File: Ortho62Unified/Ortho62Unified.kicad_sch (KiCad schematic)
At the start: 189 parts, among them J2 Conn_01x06_Socket, J3 USB_C_Receptacle_USB2.0, J5 Conn_01x06_Socket, J6 Conn_01x06_Socket, J7 Conn_01x08_Socket, J8 Conn_01x06_Socket, J9 TC2030-IDC-NL, SW1 SW_Push, SW10 SW_Push, SW11 SW_Push, SW12 SW_Push, SW13 SW_Push, SW14 SW_Push, SW15 SW_Push, SW16 SW_Push, SW17 SW_Push, SW18 SW_Push, SW19 SW_Push, SW2 SW_Push, SW20 SW_Push, SW21 SW_Push, SW22 SW_Push, SW23 SW_Push, SW24 SW_Push, SW25 SW_Push, SW26 SW_Push, SW27 SW_Push, SW28 SW_Push, SW29 SW_Push, SW3 SW_Push, SW30 SW_Push, SW31 SW_Push, SW32 SW_Push, SW33 SW_Push, SW34 SW_Push, SW35 SW_Push, SW36 SW_Push, SW37 SW_Push, SW38 SW_Push, SW39 SW_Push, SW4 SW_Push, SW40 SW_Push, SW41 SW_Push, SW42 SW_Push, SW43 SW_Push, SW44 SW_Push, SW45 SW_Push, SW46 SW_Push, SW47 SW_Push, SW48 SW_Push, SW49 SW_Push, SW5 SW_Push, SW50 SW_Push, SW51 SW_Push, SW52 SW_Push, SW53 SW_Push, SW54 SW_Push, SW55 SW_Push, SW56 SW_Push, SW57 SW_Push, SW58 SW_Push, SW59 SW_Push, SW6 SW_Push, SW60 SW_Push, SW61 SW_Push, SW62 SW_Push, SW63 SW_Push, SW64 SW_Push, SW65 SW_Push, SW66 SW_Push, SW67 SW_Push, SW68 SW_Push, SW69 SW_Push, SW7 SW_Push, SW70 SW_Push, SW71 SW_Push, SW72 SW_Push, SW73 SW_Push, SW74 OS, SW75 SW_Push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

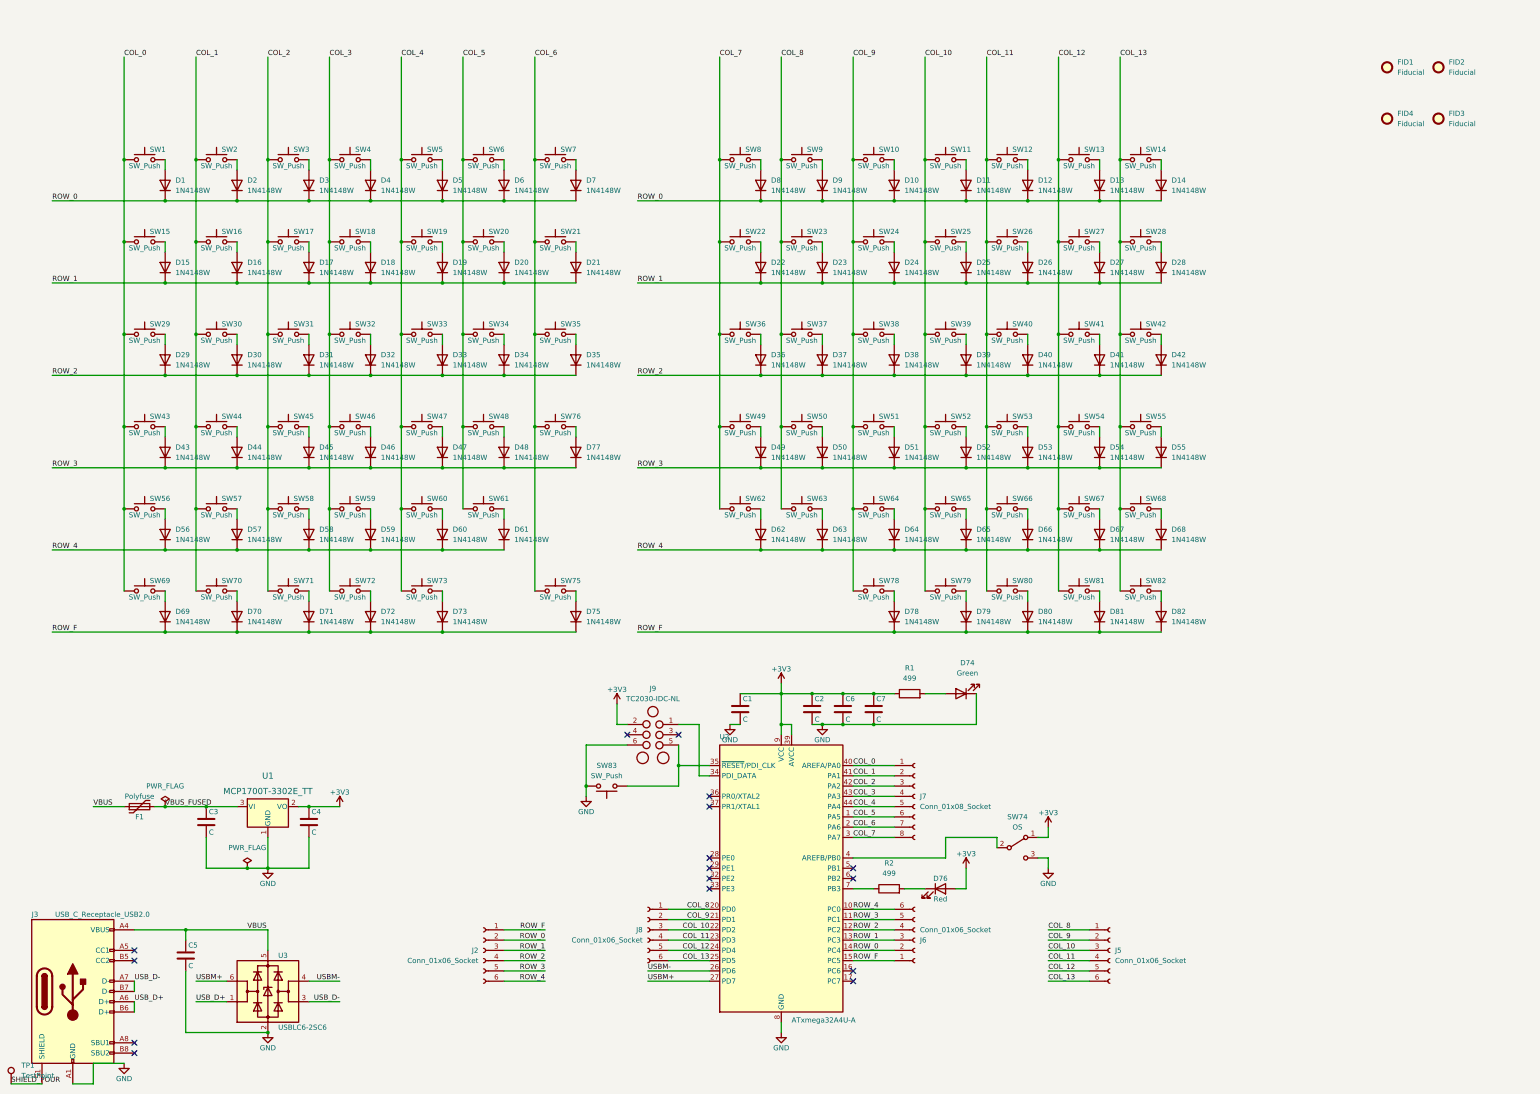
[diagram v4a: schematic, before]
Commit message: Correct spacing and kb2040 try.
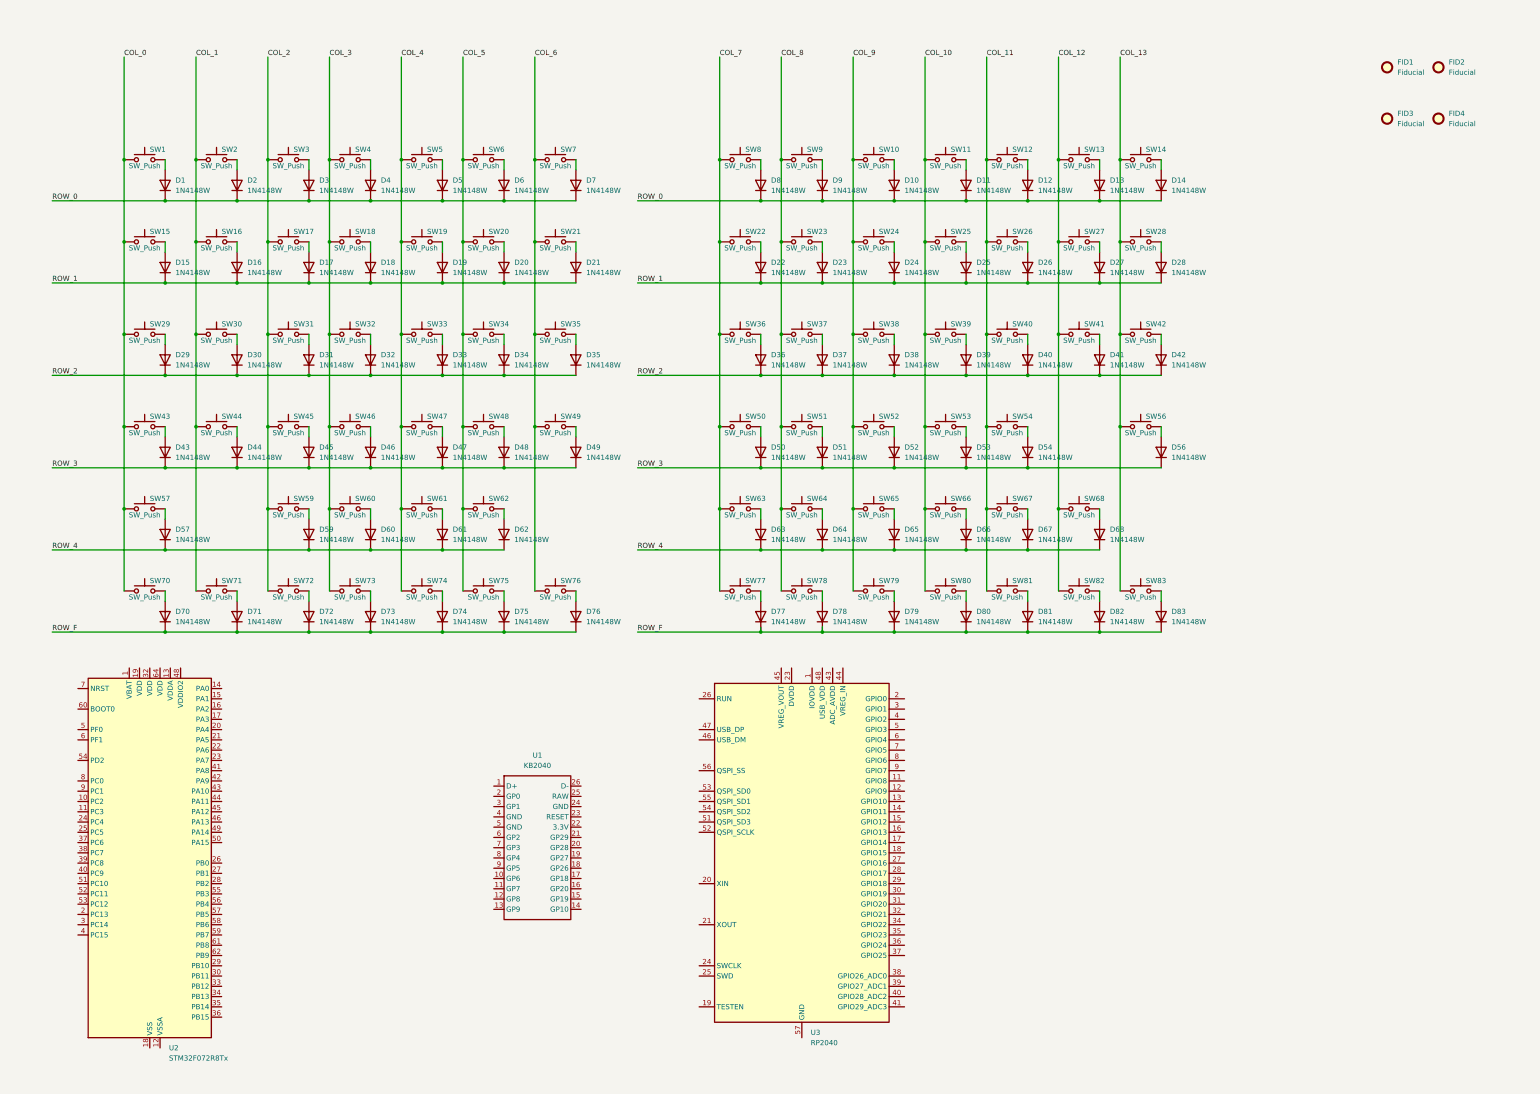
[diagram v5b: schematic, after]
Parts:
- removed C1, C2, C3, C4, C5, C6, C7: C, Capacitor_SMD:C_0603_1608Metric_Pad1.08x0.95mm_HandSolder, symbol Device:C
- removed D54, D57, D68: 1N4148W, Diode_SMD:D_SOD-123, symbol Diode:1N4148W
- removed D74: Green, LED_SMD:LED_0805_2012Metric_Pad1.15x1.40mm_HandSolder, symbol Device:LED
- removed D76: Red, LED_SMD:LED_0805_2012Metric_Pad1.15x1.40mm_HandSolder, symbol Device:LED
- removed F1: Polyfuse, Fuse:Fuse_1206_3216Metric_Pad1.42x1.75mm_HandSolder, symbol Device:Polyfuse
- removed J2, J5, J6, J8: Conn_01x06_Socket, Connector_PinHeader_1.27mm:PinHeader_1x06_P1.27mm_Vertical, symbol Connector:Conn_01x06_Socket
- removed J3: USB_C_Receptacle_USB2.0, CustomHandSolderConnectors:USB_C_Receptacle_GCT_USB4085_HandSolder_SMT, symbol Connector:USB_C_Receptacle_USB2.0
- removed J7: Conn_01x08_Socket, Connector_PinHeader_1.27mm:PinHeader_1x08_P1.27mm_Vertical, symbol Connector:Conn_01x08_Socket
- removed J9: TC2030-IDC-NL, Tag_Connect:TC2030-IDC-NL, symbol Tag-Connect:TC2030-IDC-NL
- removed R1: 499, Resistor_SMD:R_0805_2012Metric_Pad1.20x1.40mm_HandSolder, symbol Device:R
- removed R2: 499, LED_SMD:LED_0805_2012Metric_Pad1.15x1.40mm_HandSolder, symbol Device:R
- removed SW54, SW57, SW68: SW_Push, Switch_Keyboard_Kailh:SW_Kailh_Choc_V1V2_1.00u, symbol Switch:SW_Push
- removed SW74: OS, Button_Switch_SMD:SW_SPDT_CK-JS102011SAQN, symbol Switch:SW_SPDT
- removed SW83: SW_Push, Button_Switch_SMD:SW_Tactile_SPST_NO_Straight_CK_PTS636Sx25SMTRLFS, symbol Switch:SW_Push
- removed TP1: TestPoint, TestPoint:TestPoint_Pad_D1.0mm, symbol Connector:TestPoint
- removed U1: MCP1700T-3302E_TT, Package_TO_SOT_SMD:SOT-23, symbol Regulator_Linear:MCP1700x-330xxTT
- removed U2: ATxmega32A4U-A, Package_QFP:TQFP-44_10x10mm_P0.8mm, symbol MCU_Microchip_ATmega:ATxmega32A4U-A
- removed U3: USBLC6-2SC6, Package_TO_SOT_SMD:SOT-23-6, symbol Power_Protection:USBLC6-2SC6
- added D75, D77, D78: 1N4148W, Diode_SMD:D_SOD-123, symbol Diode:1N4148W
- added SW75, SW77, SW78: SW_Push, Kailh Keyboard Switches:SW_Kailh_Choc_V1V2_1.00u, symbol Switch:SW_Push
- added U1: KB2040, KB2040:Adafruit_KB2040, symbol KB2040:KB2040
- added U2: STM32F072R8Tx, Package_QFP:LQFP-64_10x10mm_P0.5mm, symbol MCU_ST_STM32F0:STM32F072R8Tx
- added U3: RP2040, Package_DFN_QFN:QFN-56-1EP_7x7mm_P0.4mm_EP3.2x3.2mm, symbol MCU_RaspberryPi:RP2040
- SW1, SW10, SW11, SW12, SW13, SW15, SW16, SW17, SW18, SW19, SW2, SW20, SW22, SW23, SW24, SW25, SW26, SW27, SW29, SW3, SW30, SW31, SW32, SW33, SW34, SW36, SW37, SW38, SW39, SW4, SW40, SW41, SW43, SW44, SW45, SW46, SW47, SW48, SW5, SW6, SW8, SW9: footprint Switch_Keyboard_Kailh:SW_Kailh_Choc_V1V2_1.00u -> Kailh Keyboard Switches:SW_Kailh_Choc_V1V2_1.00u
- SW14, SW21, SW28, SW35, SW42, SW7: footprint Switch_Keyboard_Kailh:SW_Kailh_Choc_V1V2_1.50u -> Kailh Keyboard Switches:SW_Kailh_Choc_V1V2_1.50u
- SW49: renamed from SW76; footprint Switch_Keyboard_Kailh:SW_Kailh_Choc_V1V2_1.00u -> Kailh Keyboard Switches:SW_Kailh_Choc_V1V2_1.00u
- SW50: renamed from SW49; footprint Switch_Keyboard_Kailh:SW_Kailh_Choc_V1V2_1.00u -> Kailh Keyboard Switches:SW_Kailh_Choc_V1V2_1.00u
- SW51: renamed from SW50; footprint Switch_Keyboard_Kailh:SW_Kailh_Choc_V1V2_1.00u -> Kailh Keyboard Switches:SW_Kailh_Choc_V1V2_1.00u
- SW52: renamed from SW51; footprint Switch_Keyboard_Kailh:SW_Kailh_Choc_V1V2_1.00u -> Kailh Keyboard Switches:SW_Kailh_Choc_V1V2_1.00u
- SW53: renamed from SW52; footprint Switch_Keyboard_Kailh:SW_Kailh_Choc_V1V2_1.00u -> Kailh Keyboard Switches:SW_Kailh_Choc_V1V2_1.00u
- SW54: renamed from SW53; footprint Switch_Keyboard_Kailh:SW_Kailh_Choc_V1V2_1.00u -> Kailh Keyboard Switches:SW_Kailh_Choc_V1V2_1.00u
- SW56: renamed from SW55; footprint Switch_Keyboard_Kailh:SW_Kailh_Choc_V1V2_1.00u -> Kailh Keyboard Switches:SW_Kailh_Choc_V1V2_2.00u
- SW57: renamed from SW56; footprint Switch_Keyboard_Kailh:SW_Kailh_Choc_V1V2_1.50u -> Kailh Keyboard Switches:SW_Kailh_Choc_V1V2_2.00u
- SW59: renamed from SW58; footprint Switch_Keyboard_Kailh:SW_Kailh_Choc_V1V2_1.00u -> Kailh Keyboard Switches:SW_Kailh_Choc_V1V2_1.00u
- SW60: renamed from SW59; footprint Switch_Keyboard_Kailh:SW_Kailh_Choc_V1V2_1.00u -> Kailh Keyboard Switches:SW_Kailh_Choc_V1V2_1.00u
- SW61: renamed from SW60; footprint Switch_Keyboard_Kailh:SW_Kailh_Choc_V1V2_1.00u -> Kailh Keyboard Switches:SW_Kailh_Choc_V1V2_1.00u
- SW62: renamed from SW61; footprint Switch_Keyboard_Kailh:SW_Kailh_Choc_V1V2_1.50u -> Kailh Keyboard Switches:SW_Kailh_Choc_V1V2_1.50u
- SW63: renamed from SW62; footprint Switch_Keyboard_Kailh:SW_Kailh_Choc_V1V2_1.00u -> Kailh Keyboard Switches:SW_Kailh_Choc_V1V2_1.00u
- SW64: renamed from SW63; footprint Switch_Keyboard_Kailh:SW_Kailh_Choc_V1V2_1.50u -> Kailh Keyboard Switches:SW_Kailh_Choc_V1V2_1.50u
- SW65: renamed from SW64; footprint Switch_Keyboard_Kailh:SW_Kailh_Choc_V1V2_1.00u -> Kailh Keyboard Switches:SW_Kailh_Choc_V1V2_1.00u
- SW66: renamed from SW65; footprint Switch_Keyboard_Kailh:SW_Kailh_Choc_V1V2_1.00u -> Kailh Keyboard Switches:SW_Kailh_Choc_V1V2_1.00u
- SW67: renamed from SW66; footprint Switch_Keyboard_Kailh:SW_Kailh_Choc_V1V2_1.00u -> Kailh Keyboard Switches:SW_Kailh_Choc_V1V2_1.00u
- SW68: renamed from SW67; footprint Switch_Keyboard_Kailh:SW_Kailh_Choc_V1V2_1.50u -> Kailh Keyboard Switches:SW_Kailh_Choc_V1V2_1.50u
- SW70: renamed from SW69; footprint Switch_Keyboard_Kailh:SW_Kailh_Choc_V1V2_1.00u -> Kailh Keyboard Switches:SW_Kailh_Choc_V1V2_1.00u
- SW71: renamed from SW70; footprint Switch_Keyboard_Kailh:SW_Kailh_Choc_V1V2_1.00u -> Kailh Keyboard Switches:SW_Kailh_Choc_V1V2_1.00u
- SW72: renamed from SW71; footprint Switch_Keyboard_Kailh:SW_Kailh_Choc_V1V2_1.00u -> Kailh Keyboard Switches:SW_Kailh_Choc_V1V2_1.00u
- SW73: renamed from SW72; footprint Switch_Keyboard_Kailh:SW_Kailh_Choc_V1V2_1.00u -> Kailh Keyboard Switches:SW_Kailh_Choc_V1V2_1.00u
- SW74: renamed from SW73; footprint Switch_Keyboard_Kailh:SW_Kailh_Choc_V1V2_1.00u -> Kailh Keyboard Switches:SW_Kailh_Choc_V1V2_1.00u
- SW76: renamed from SW75; footprint Switch_Keyboard_Kailh:SW_Kailh_Choc_V1V2_1.50u -> Kailh Keyboard Switches:SW_Kailh_Choc_V1V2_1.50u
- SW79: renamed from SW78; footprint Switch_Keyboard_Kailh:SW_Kailh_Choc_V1V2_1.00u -> Kailh Keyboard Switches:SW_Kailh_Choc_V1V2_1.00u
- SW80: renamed from SW79; footprint Switch_Keyboard_Kailh:SW_Kailh_Choc_V1V2_1.00u -> Kailh Keyboard Switches:SW_Kailh_Choc_V1V2_1.00u
- SW81: renamed from SW80; footprint Switch_Keyboard_Kailh:SW_Kailh_Choc_V1V2_1.00u -> Kailh Keyboard Switches:SW_Kailh_Choc_V1V2_1.00u
- SW82: renamed from SW81; footprint Switch_Keyboard_Kailh:SW_Kailh_Choc_V1V2_1.00u -> Kailh Keyboard Switches:SW_Kailh_Choc_V1V2_1.00u
- SW83: renamed from SW82; footprint Switch_Keyboard_Kailh:SW_Kailh_Choc_V1V2_1.50u -> Kailh Keyboard Switches:SW_Kailh_Choc_V1V2_1.50u
- renumbered D77 to D49, D49 to D50, D50 to D51, D51 to D52, D52 to D53, D53 to D54, D55 to D56, D56 to D57, D58 to D59, D59 to D60, D60 to D61, D61 to D62, D62 to D63, D63 to D64, D64 to D65, D65 to D66, D66 to D67, D67 to D68, D69 to D70, D70 to D71, D71 to D72, D72 to D73, D73 to D74, D75 to D76, D78 to D79, D79 to D80, D80 to D81, D81 to D82, D82 to D83, FID4 to FID3, FID3 to FID4
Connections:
- net COL_5: now also SW75.1
- net COL_7: now also SW77.1
- net COL_8: now also SW78.1
- net ROW_F: now also D75.1 (K), D77.1 (K), D78.1 (K)
- new net: U2.18 (VSS), U2.31 (VSS), U2.47 (VSS), U2.63 (VSS)
- new net: D75.2 (A), SW75.2
- new net: D77.2 (A), SW77.2
- new net: D78.2 (A), SW78.2
- new net: U3.1 (IOVDD), U3.10 (IOVDD), U3.22 (IOVDD), U3.33 (IOVDD), U3.42 (IOVDD), U3.49 (IOVDD)
- new net: U3.23 (DVDD), U3.50 (DVDD)
- no-connect marks 16 -> 0
